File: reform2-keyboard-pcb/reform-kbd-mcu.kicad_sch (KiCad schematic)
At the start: 20 parts, among them J1 USB, J2 UART, J3 AUX, J4 MCU Airwire USB, J6 AUX, SW101 SW_SPDT, U1 itsy-32u4-3v3

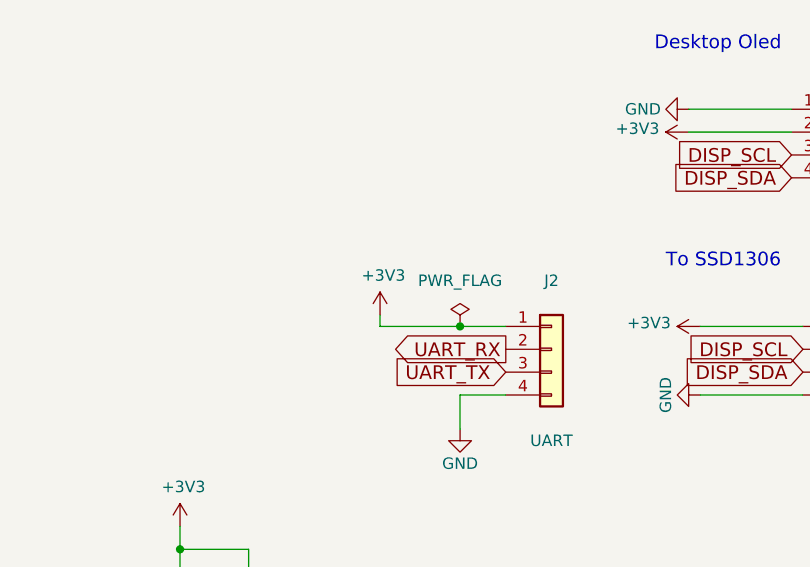
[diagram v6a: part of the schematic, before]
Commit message: add jumper on serial 3v
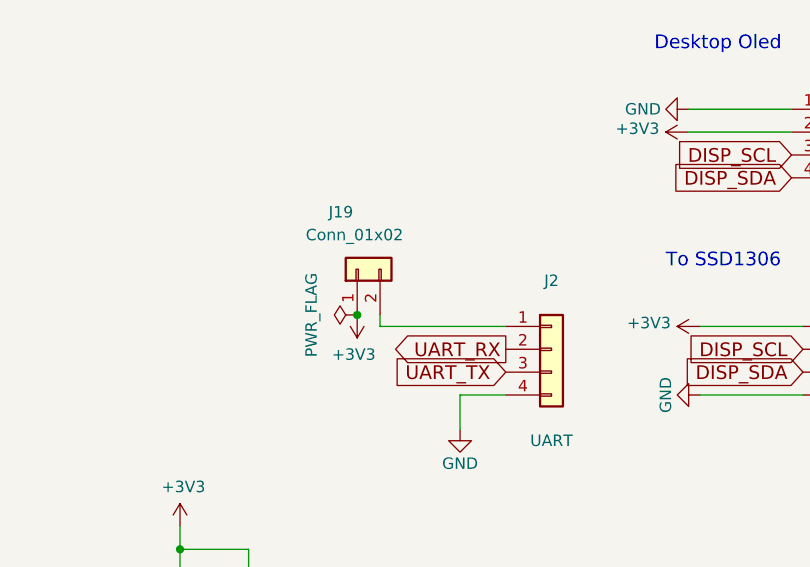
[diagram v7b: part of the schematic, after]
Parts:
- added J19: Conn_01x02, Connector_PinSocket_2.54mm:PinSocket_1x02_P2.54mm_Vertical, symbol Connector_Generic:Conn_01x02
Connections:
- net +3V3: now also J19.1 (Pin_1); no longer J2.1 (Pin_1)
- new net: J19.2 (Pin_2), J2.1 (Pin_1)
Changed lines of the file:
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@@
   (junction (at 96.52 182.88) (diameter 0) (color 0 0 0 0)
   )
+  (junction (at 184.15 130.81) (diameter 0) (color 0 0 0 0)
+  )
   (junction (at 122.555 33.02) (diameter 0) (color 0 0 0 0)
   )
@@
   )
   (junction (at 189.23 73.025) (diameter 0) (color 0 0 0 0)
-  )
-  (junction (at 195.58 132.08) (diameter 0) (color 0 0 0 0)
   )
   (junction (at 106.68 182.88) (diameter 0) (color 0 0 0 0)
@@
     (stroke (width 0) (type default) (color 0 0 0 0))
   )
-  (wire (pts (xy 195.58 132.08) (xy 200.66 132.08))
-    (stroke (width 0) (type default) (color 0 0 0 0))
-  )
   (wire (pts (xy 189.23 73.025) (xy 189.23 73.66))
     (stroke (width 0) (type default) (color 0 0 0 0))
@@
     (stroke (width 0) (type default) (color 0 0 0 0))
   )
-  (wire (pts (xy 186.69 132.08) (xy 195.58 132.08))
+  (wire (pts (xy 186.69 132.08) (xy 200.66 132.08))
     (stroke (width 0) (type default) (color 0 0 0 0))
   )
@@
     (pin "1")
   )
-  (symbol (lib_id "power:+3V3") (at 186.69 130.81 0) (unit 1)
-    (in_bom yes) (on_board yes)
-    (property "Reference" "#PWR016" (id 0) (at 186.69 134.62 0)
-      (effects (font (size 1.27 1.27)) hide)
-    )
-    (property "Value" "+3V3" (id 1) (at 187.071 126.4158 0))
-    (property "Footprint" "" (id 2) (at 186.69 130.81 0)
-      (effects (font (size 1.27 1.27)) hide)
-    )
-    (property "Datasheet" "" (id 3) (at 186.69 130.81 0)
-      (effects (font (size 1.27 1.27)) hide)
-    )
-    (pin "1")
-  )
-  (symbol (lib_id "power:PWR_FLAG") (at 195.58 132.08 0) (unit 1)
-    (in_bom yes) (on_board yes)
-    (property "Reference" "#FLG02" (id 0) (at 195.58 130.175 0)
-      (effects (font (size 1.27 1.27)) hide)
-    )
-    (property "Value" "PWR_FLAG" (id 1) (at 195.58 127 0))
-    (property "Footprint" "" (id 2) (at 195.58 132.08 0)
-      (effects (font (size 1.27 1.27)) hide)
-    )
-    (property "Datasheet" "~" (id 3) (at 195.58 132.08 0)
+  (symbol (lib_id "power:+3V3") (at 184.15 130.81 180) (unit 1)
+    (in_bom yes) (on_board yes)
+    (property "Reference" "#PWR016" (id 0) (at 184.15 127 0)
+      (effects (font (size 1.27 1.27)) hide)
+    )
+    (property "Value" "+3V3" (id 1) (at 183.769 135.2042 0))
+    (property "Footprint" "" (id 2) (at 184.15 130.81 0)
+      (effects (font (size 1.27 1.27)) hide)
+    )
+    (property "Datasheet" "" (id 3) (at 184.15 130.81 0)
+      (effects (font (size 1.27 1.27)) hide)
+    )
+    (pin "1")
+  )
+  (symbol (lib_id "power:PWR_FLAG") (at 184.15 130.81 90) (unit 1)
+    (in_bom yes) (on_board yes)
+    (property "Reference" "#FLG02" (id 0) (at 182.245 130.81 0)
+      (effects (font (size 1.27 1.27)) hide)
+    )
+    (property "Value" "PWR_FLAG" (id 1) (at 179.07 130.81 0))
+    (property "Footprint" "" (id 2) (at 184.15 130.81 0)
+      (effects (font (size 1.27 1.27)) hide)
+    )
+    (property "Datasheet" "~" (id 3) (at 184.15 130.81 0)
       (effects (font (size 1.27 1.27)) hide)
     )
@@
     (pin "1")
   )
+  (symbol (lib_id "Connector_Generic:Conn_01x02") (at 184.15 125.73 90) (unit 1)
+    (in_bom yes) (on_board yes)
+    (property "Reference" "J19" (id 0) (at 180.975 119.38 90)
+      (effects (font (size 1.27 1.27)) (justify right))
+    )
+    (property "Value" "Conn_01x02" (id 1) (at 178.435 121.92 90)
+      (effects (font (size 1.27 1.27)) (justify right))
+    )
+    (property "Footprint" "Connector_PinSocket_2.54mm:PinSocket_1x02_P2.54mm_Vertical" (id 2) (at 184.15 125.73 0)
+      (effects (font (size 1.27 1.27)) hide)
+    )
+    (property "Datasheet" "~" (id 3) (at 184.15 125.73 0)
+      (effects (font (size 1.27 1.27)) hide)
+    )
+    (pin "1")
+    (pin "2")
+  )
   (symbol (lib_id "Switch:SW_SPDT") (at 208.28 55.88 0) (unit 1)
